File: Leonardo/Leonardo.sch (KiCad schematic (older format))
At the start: 47 parts, among them J1 Conn_01x08_Female, J2 Conn_01x06_Female, J3 Conn_01x10_Female, J4 Conn_01x08_Female, J5 Conn_02x03_Odd_Even, J6 USB_Micro, J7 Barrel_Jack, Q1 FDN340P, SW1 Reset, U1 LMV358IDGKR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

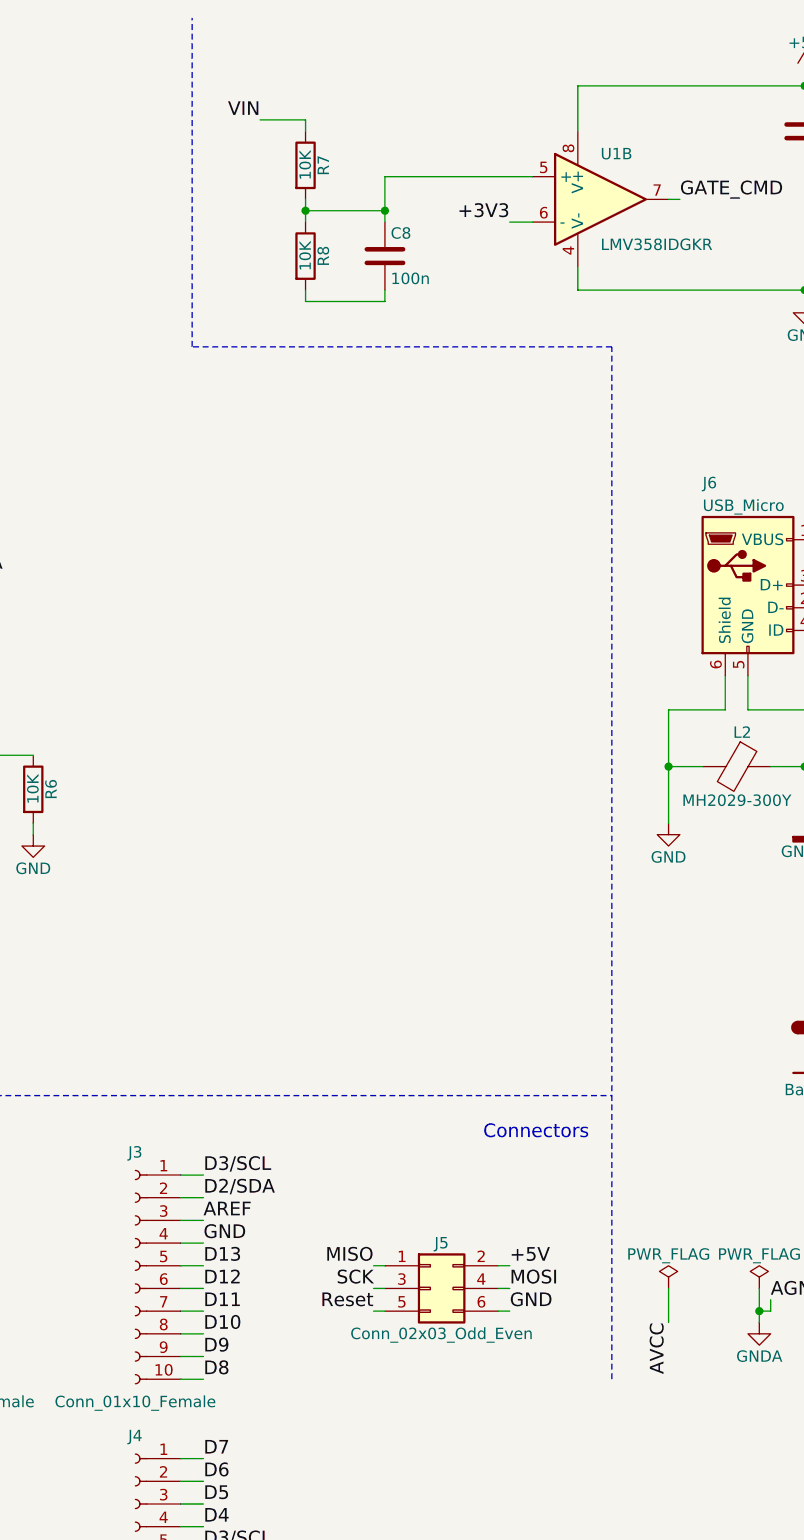
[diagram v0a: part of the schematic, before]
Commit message: Fixed missing GND
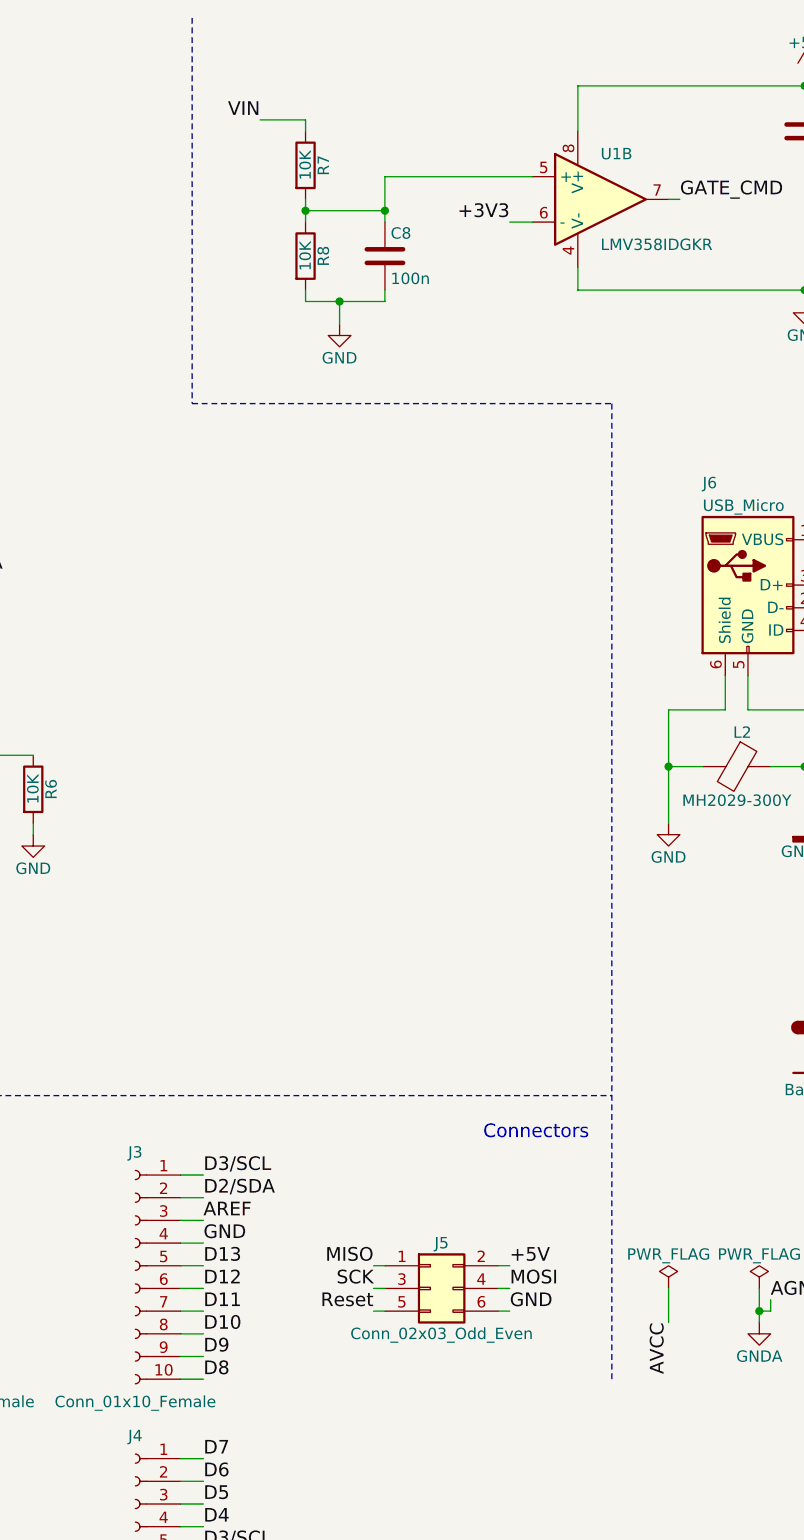
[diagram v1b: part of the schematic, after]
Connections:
- net GND: now also C8.2, R8.2

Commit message: Filled in the component footprints
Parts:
- removed SW1: Reset, symbol SW_Push_Dual
- removed Y1: 16MHz, symbol Crystal_GND23
- added SW1: TL3342, Buttons_Switches_SMD:SW_SPST_TL3342, symbol SW_Push
- added Y1: 16MHz, Crystals:Crystal_SMD_5032-4pin_5.0x3.2mm, symbol Crystal_GND24
- C1, C10, C12: footprint (none) -> Capacitors_SMD:CP_Elec_5x4.5
- C11, C13, C2, C3, C4, C5, C6, C7, C8, C9, L1, L2: footprint (none) -> Capacitors_SMD:C_0805
- D1, D2, D3, D4: footprint (none) -> LEDs:LED_0805
- D5: footprint (none) -> Diodes_SMD:D_0805
- F1: footprint (none) -> Fuse_Holders_and_Fuses:Fuse_SMD1206_Reflow
- J1, J4: footprint (none) -> Socket_Strips:Socket_Strip_Straight_1x08_Pitch2.54mm
- J2: footprint (none) -> Socket_Strips:Socket_Strip_Straight_1x06_Pitch2.54mm
- J3: footprint (none) -> Socket_Strips:Socket_Strip_Straight_1x10_Pitch2.54mm
- J5: footprint (none) -> Pin_Headers:Pin_Header_Straight_2x03_Pitch2.54mm
- J6: footprint (none) -> Connectors:USB_Micro-B
- J7: footprint (none) -> DC10LP socket:DC10LP socket
- R1, R10, R2, R3, R4, R5, R6, R7, R8, R9: footprint (none) -> Resistors_SMD:R_0805
- RV1, RV2: footprint (none) -> Resistors_SMD:R_0603
- U1: footprint (none) -> Housings_SSOP:TSSOP-8_3x3mm_Pitch0.65mm
- U2: footprint TQFP44 -> Housings_QFP:LQFP-44_10x10mm_Pitch0.8mm
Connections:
- net GND: now also SW1.2, Y1.2, Y1.4
- net Reset: now also SW1.1
- net at C4.1, U2.16 (XTAL2): now also Y1.1
- net at C3.1, U2.17 (XTAL1): now also Y1.3

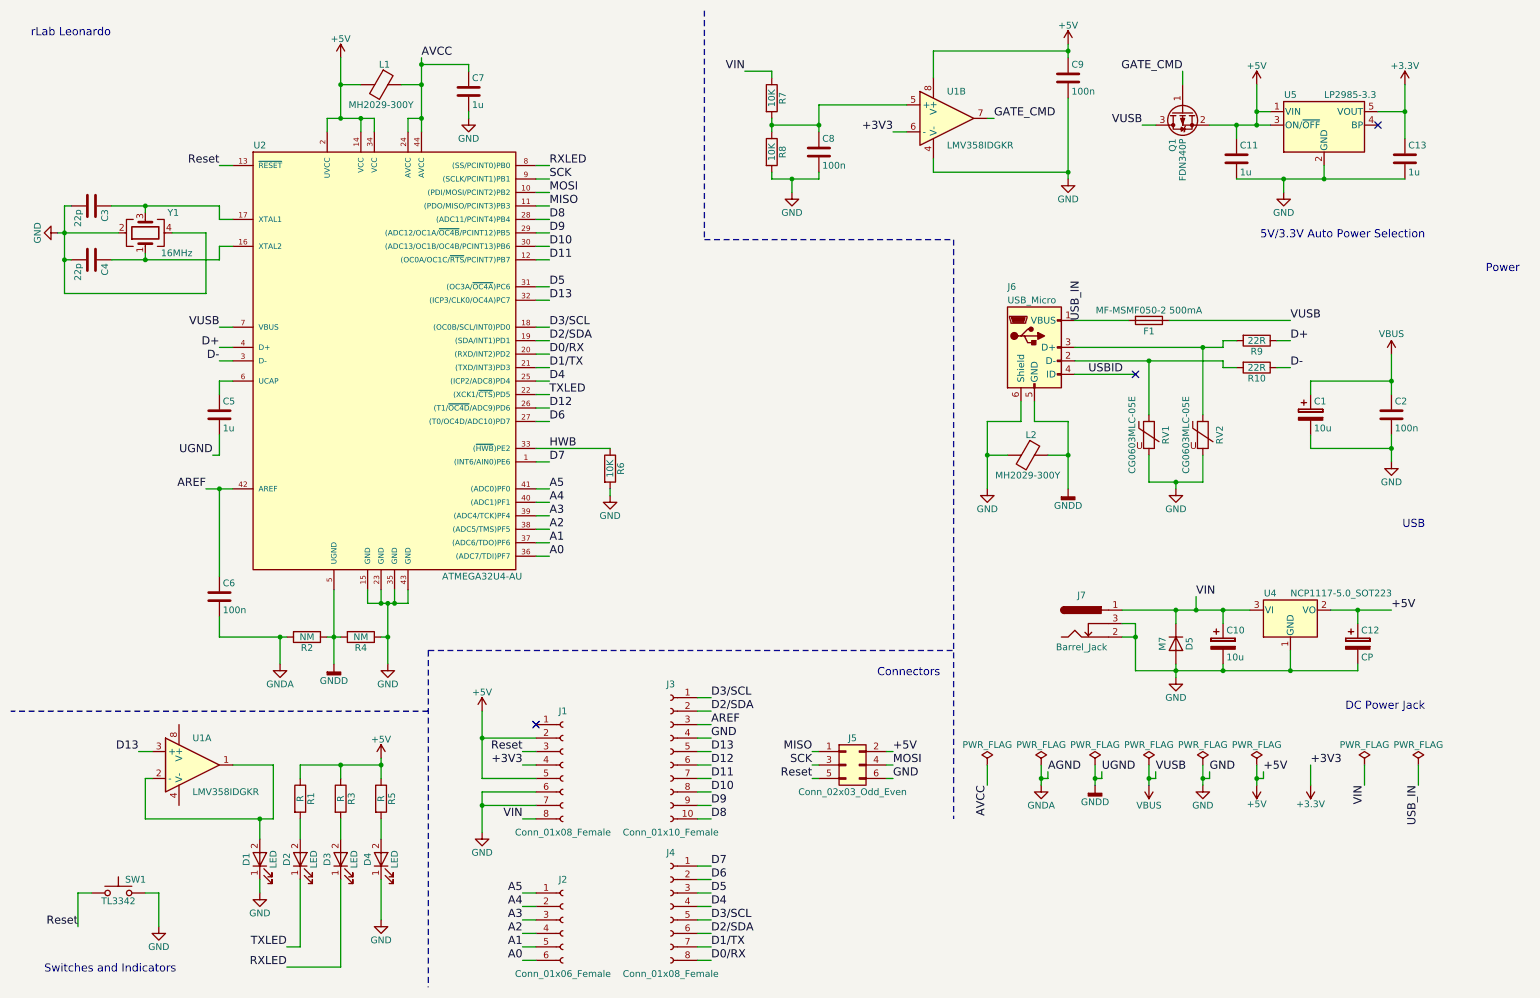
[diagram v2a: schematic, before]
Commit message: Added a few missing resistors
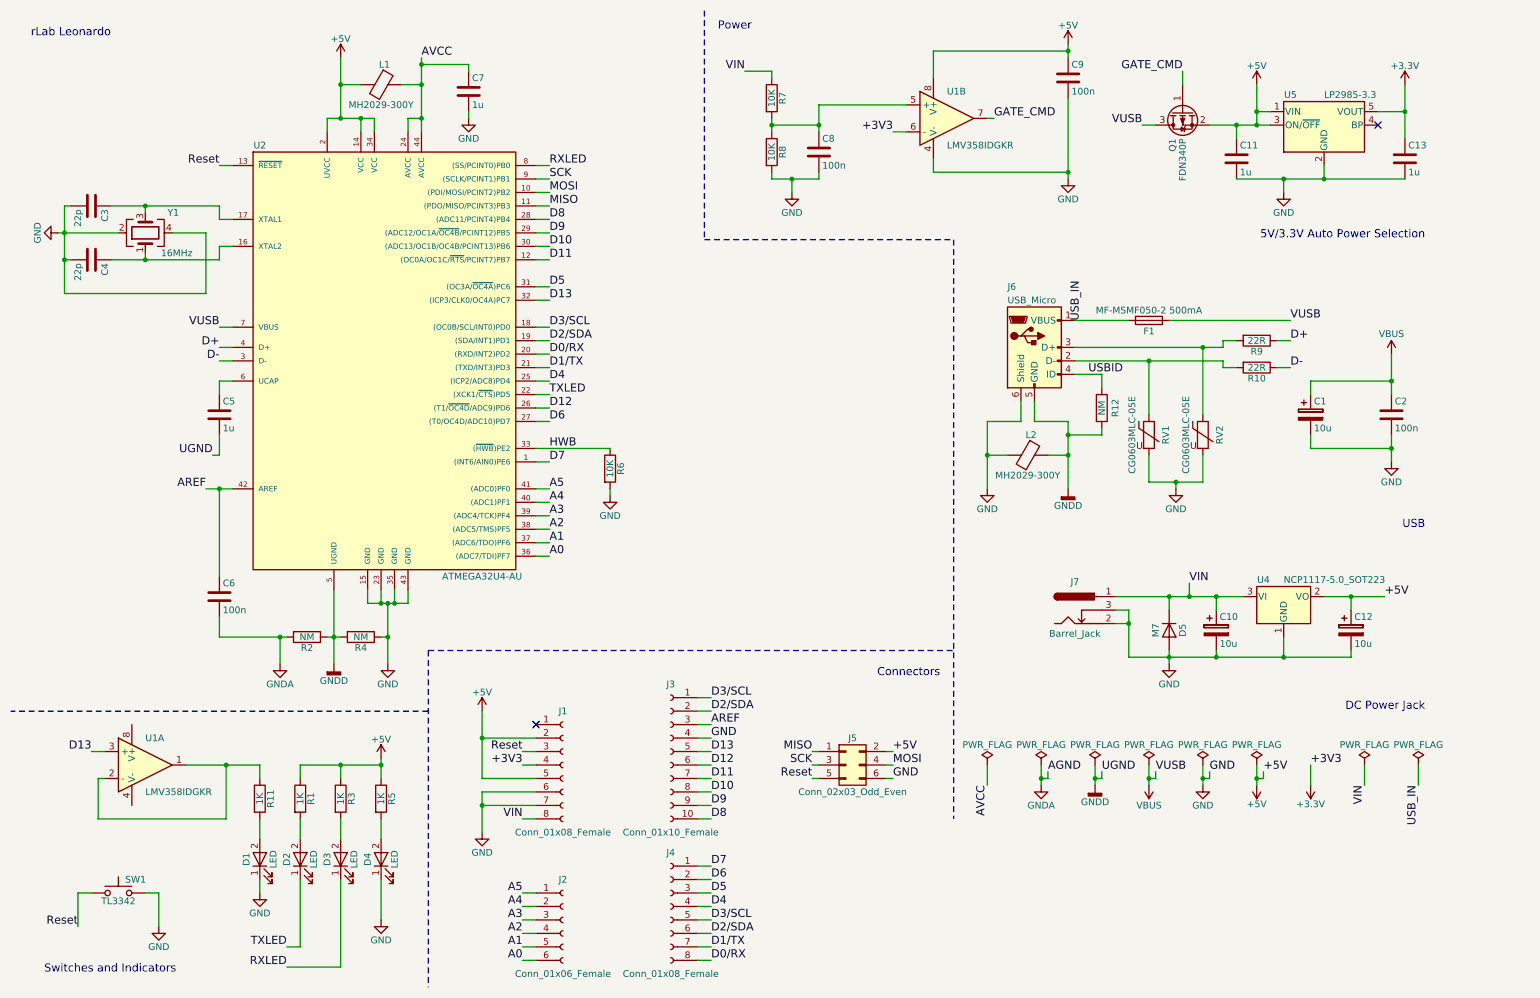
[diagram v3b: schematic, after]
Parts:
- added R11: 1K, Resistors_SMD:R_0805, symbol R
- added R12: NM, Resistors_SMD:R_0805, symbol R
- C12: value CP -> 10u
- R1, R3, R5: value R -> 1K
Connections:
- net GNDD: now also R12.2
- net USBID: now also R12.1
- net at U1.1, U1.2 (-): now also R11.1; no longer D1.2 (A)
- new net: D1.2 (A), R11.2
- no-connect marks 3 -> 2
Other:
- moved on the sheet: C10, C12, D5, J7, U1A, U4
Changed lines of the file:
@@
 L LM2904 U1
 U 1 1 59B84AA6
-P 1850 6100
-F 0 "U1" H 1850 6300 50  0000 L CNN
-F 1 "LMV358IDGKR" H 1850 5900 50  0000 L CNN
-F 2 "Housings_SSOP:TSSOP-8_3x3mm_Pitch0.65mm" H 1850 6100 50  0001 C CNN
-F 3 "" H 1850 6100 50  0001 C CNN
-	1    1850 6100
+P 1500 6100
+F 0 "U1" H 1500 6300 50  0000 L CNN
+F 1 "LMV358IDGKR" H 1500 5900 50  0000 L CNN
+F 2 "Housings_SSOP:TSSOP-8_3x3mm_Pitch0.65mm" H 1500 6100 50  0001 C CNN
+F 3 "" H 1500 6100 50  0001 C CNN
+	1    1500 6100
 	1    0    0    -1
 $EndComp
@@
 P 2650 6350
 F 0 "R1" V 2730 6350 50  0000 C CNN
-F 1 "R" V 2650 6350 50  0000 C CNN
+F 1 "1K" V 2650 6350 50  0000 C CNN
 F 2 "Resistors_SMD:R_0805" V 2580 6350 50  0001 C CNN
 F 3 "" H 2650 6350 50  0001 C CNN
@@
 P 2950 6350
 F 0 "R3" V 3030 6350 50  0000 C CNN
-F 1 "R" V 2950 6350 50  0000 C CNN
+F 1 "1K" V 2950 6350 50  0000 C CNN
 F 2 "Resistors_SMD:R_0805" V 2880 6350 50  0001 C CNN
 F 3 "" H 2950 6350 50  0001 C CNN
@@
 P 3250 6350
 F 0 "R5" V 3330 6350 50  0000 C CNN
-F 1 "R" V 3250 6350 50  0000 C CNN
+F 1 "1K" V 3250 6350 50  0000 C CNN
 F 2 "Resistors_SMD:R_0805" V 3180 6350 50  0001 C CNN
 F 3 "" H 3250 6350 50  0001 C CNN
@@
 	1    0    0    -1
 $EndComp
-Text Label 1450 6000 2    60   ~ 0
+Text Label 1100 6000 2    60   ~ 0
 D13
 Text Label 9400 6150 0    60   ~ 0
@@
 L Barrel_Jack J7
 U 1 1 59BDBFEB
-P 8450 5050
-F 0 "J7" H 8450 5260 50  0000 C CNN
-F 1 "Barrel_Jack" H 8450 4875 50  0000 C CNN
-F 2 "DC10LP socket:DC10LP socket" H 8500 5010 50  0001 C CNN
-F 3 "" H 8500 5010 50  0001 C CNN
-	1    8450 5050
+P 8400 4950
+F 0 "J7" H 8400 5160 50  0000 C CNN
+F 1 "Barrel_Jack" H 8400 4775 50  0000 C CNN
+F 2 "DC10LP socket:DC10LP socket" H 8450 4910 50  0001 C CNN
+F 3 "" H 8450 4910 50  0001 C CNN
+	1    8400 4950
 	1    0    0    -1
 $EndComp
@@
 L GND #PWR023
 U 1 1 59BDC2A6
-P 9150 5450
-F 0 "#PWR023" H 9150 5200 50  0001 C CNN
-F 1 "GND" H 9150 5300 50  0000 C CNN
-F 2 "" H 9150 5450 50  0001 C CNN
-F 3 "" H 9150 5450 50  0001 C CNN
-	1    9150 5450
+P 9100 5350
+F 0 "#PWR023" H 9100 5100 50  0001 C CNN
+F 1 "GND" H 9100 5200 50  0000 C CNN
+F 2 "" H 9100 5350 50  0001 C CNN
+F 3 "" H 9100 5350 50  0001 C CNN
+	1    9100 5350
 	1    0    0    -1
 $EndComp
@@
 L D D5
 U 1 1 59BDC41B
-P 9150 5200
-F 0 "D5" H 9150 5300 50  0000 C CNN
-F 1 "M7" H 9150 5100 50  0000 C CNN
-F 2 "Diodes_SMD:D_0805" H 9150 5200 50  0001 C CNN
-F 3 "" H 9150 5200 50  0001 C CNN
-	1    9150 5200
+P 9100 5100
+F 0 "D5" H 9100 5200 50  0000 C CNN
+F 1 "M7" H 9100 5000 50  0000 C CNN
+F 2 "Diodes_SMD:D_0805" H 9100 5100 50  0001 C CNN
+F 3 "" H 9100 5100 50  0001 C CNN
+	1    9100 5100
 	0    1    1    0
 $EndComp
@@
 L CP C10
 U 1 1 59BDC54A
-P 9500 5200
-F 0 "C10" H 9525 5300 50  0000 L CNN
-F 1 "10u" H 9525 5100 50  0000 L CNN
-F 2 "Capacitors_SMD:CP_Elec_5x4.5" H 9538 5050 50  0001 C CNN
-F 3 "" H 9500 5200 50  0001 C CNN
-	1    9500 5200
+P 9450 5100
+F 0 "C10" H 9475 5200 50  0000 L CNN
+F 1 "10u" H 9475 5000 50  0000 L CNN
+F 2 "Capacitors_SMD:CP_Elec_5x4.5" H 9488 4950 50  0001 C CNN
+F 3 "" H 9450 5100 50  0001 C CNN
+	1    9450 5100
 	1    0    0    -1
 $EndComp
@@
 L NCP1117-5.0_SOT223 U4
 U 1 1 59BDC910
-P 10000 4950
-F 0 "U4" H 9850 5075 50  0000 C CNN
-F 1 "NCP1117-5.0_SOT223" H 10000 5075 50  0000 L CNN
-F 2 "TO_SOT_Packages_SMD:SOT-223-3Lead_TabPin2" H 10000 5150 50  0001 C CNN
-F 3 "" H 10100 4700 50  0001 C CNN
-	1    10000 4950
+P 9950 4850
+F 0 "U4" H 9800 4975 50  0000 C CNN
+F 1 "NCP1117-5.0_SOT223" H 9950 4975 50  0000 L CNN
+F 2 "TO_SOT_Packages_SMD:SOT-223-3Lead_TabPin2" H 9950 5050 50  0001 C CNN
+F 3 "" H 10050 4600 50  0001 C CNN
+	1    9950 4850
 	1    0    0    -1
 $EndComp
@@
 L CP C12
 U 1 1 59BDC9A7
-P 10500 5200
-F 0 "C12" H 10525 5300 50  0000 L CNN
-F 1 "CP" H 10525 5100 50  0000 L CNN
-F 2 "Capacitors_SMD:CP_Elec_5x4.5" H 10538 5050 50  0001 C CNN
-F 3 "" H 10500 5200 50  0001 C CNN
-	1    10500 5200
-	1    0    0    -1
-$EndComp
-Text Label 10750 4950 0    60   ~ 0
+P 10450 5100
+F 0 "C12" H 10475 5200 50  0000 L CNN
+F 1 "10u" H 10475 5000 50  0000 L CNN
+F 2 "Capacitors_SMD:CP_Elec_5x4.5" H 10488 4950 50  0001 C CNN
+F 3 "" H 10450 5100 50  0001 C CNN
+	1    10450 5100
+	1    0    0    -1
+$EndComp
+Text Label 10700 4850 0    60   ~ 0
 +5V
 Text Notes 750  7650 0    60   ~ 0
 Switches and Indicators\n
-Text Notes 11450 2450 0    60   ~ 0
+Text Notes 5750 650  0    60   ~ 0
 Power\n
 Text Notes 11000 4350 2    60   ~ 0
@@
 Text Notes 650  700  0    60   ~ 0
 rLab Leonardo\n
-Text Label 9300 4850 0    60   ~ 0
+Text Label 9250 4750 0    60   ~ 0
 VIN
 $Comp
@@
 Text Label 10950 6250 3    60   ~ 0
 USB_IN
-NoConn ~ 8850 3200
 $Comp
 L GND #PWR039
@@
 	2350 6950 2350 7050
 Wire Wire Line
-	2150 6100 2450 6100
-Wire Wire Line
-	2450 6100 2450 6500
-Wire Wire Line
-	2450 6500 1500 6500
-Wire Wire Line
-	1500 6500 1500 6200
-Wire Wire Line
-	1500 6200 1550 6200
+	1800 6100 2350 6100
+Wire Wire Line
+	2100 6100 2100 6500
+Wire Wire Line
+	2100 6500 1150 6500
+Wire Wire Line
+	1150 6500 1150 6200
+Wire Wire Line
+	1150 6200 1200 6200
 Wire Wire Line
 	9400 6150 9400 6200
@@
 Connection ~ 8350 3800
 Wire Wire Line
-	8400 3200 8850 3200
-Wire Wire Line
 	8950 3800 8950 4000
 Wire Wire Line
@@
 	10000 2800 9100 2800
 Wire Wire Line
-	8750 5050 8850 5050
-Wire Wire Line
-	8850 5050 8850 5400
-Wire Wire Line
-	8750 5150 8850 5150
-Connection ~ 8850 5150
-Wire Wire Line
-	8850 5400 10500 5400
-Wire Wire Line
-	9500 5400 9500 5350
-Wire Wire Line
-	9150 5350 9150 5450
-Connection ~ 9150 5400
-Wire Wire Line
-	8750 4950 9700 4950
-Wire Wire Line
-	10300 4950 10750 4950
-Wire Wire Line
-	10500 5050 10500 4950
-Connection ~ 10500 4950
-Wire Wire Line
-	9500 5050 9500 4950
-Connection ~ 9500 4950
-Wire Wire Line
-	9150 5050 9150 4950
-Connection ~ 9150 4950
-Wire Wire Line
-	10500 5400 10500 5350
-Connection ~ 9500 5400
-Wire Wire Line
-	10000 5250 10000 5400
-Connection ~ 10000 5400
+	8700 4950 8800 4950
+Wire Wire Line
+	8800 4950 8800 5300
+Wire Wire Line
+	8700 5050 8800 5050
+Connection ~ 8800 5050
+Wire Wire Line
+	8800 5300 10450 5300
+Wire Wire Line
+	9450 5300 9450 5250
+Wire Wire Line
+	9100 5250 9100 5350
+Connection ~ 9100 5300
+Wire Wire Line
+	8700 4850 9650 4850
+Wire Wire Line
+	10250 4850 10700 4850
+Wire Wire Line
+	10450 4950 10450 4850
+Connection ~ 10450 4850
+Wire Wire Line
+	9450 4950 9450 4850
+Connection ~ 9450 4850
+Wire Wire Line
+	9100 4950 9100 4850
+Connection ~ 9100 4850
+Wire Wire Line
+	10450 5300 10450 5250
+Connection ~ 9450 5300
+Wire Wire Line
+	9950 5150 9950 5300
+Connection ~ 9950 5300
 Wire Wire Line
 	3450 4900 3150 4900
@@
 	2650 6100 3250 6100
 Wire Wire Line
-	1550 6000 1450 6000
-Wire Wire Line
-	2350 6650 2350 6500
-Connection ~ 2350 6500
+	1200 6000 1100 6000
 Wire Notes Line
 	3600 5250 3600 7750
@@
 	3600 5250 7500 5250
 Wire Wire Line
-	9300 4950 9300 4850
-Connection ~ 9300 4950
+	9250 4850 9250 4750
+Connection ~ 9250 4850
 Wire Wire Line
 	10550 6250 10550 6100
@@
 	0    -1   -1   0
 $EndComp
+$Comp
+L R R11
+U 1 1 59C6D630
+P 2350 6350
+F 0 "R11" V 2430 6350 50  0000 C CNN
+F 1 "1K" V 2350 6350 50  0000 C CNN
+F 2 "Resistors_SMD:R_0805" V 2280 6350 50  0001 C CNN
+F 3 "" H 2350 6350 50  0001 C CNN
+	1    2350 6350
+	1    0    0    -1
+$EndComp
+Wire Wire Line
+	2350 6500 2350 6650
+Wire Wire Line
+	2350 6100 2350 6200
+Connection ~ 2100 6100
+$Comp
+L R R12
+U 1 1 59C6F210
+P 8600 3450
+F 0 "R12" V 8700 3450 50  0000 C CNN
+F 1 "NM" V 8600 3450 50  0000 C CNN
+F 2 "Resistors_SMD:R_0805" V 8530 3450 50  0001 C CNN
+F 3 "" H 8600 3450 50  0001 C CNN
+	1    8600 3450
+	1    0    0    -1
+$EndComp
+Wire Wire Line
+	8350 3650 8600 3650
+Wire Wire Line
+	8600 3650 8600 3600
+Connection ~ 8350 3650
+Wire Wire Line
+	8600 3300 8600 3200
+Wire Wire Line
+	8600 3200 8400 3200
 $EndSCHEMATC
